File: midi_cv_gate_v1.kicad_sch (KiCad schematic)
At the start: 27 parts, among them J1 Conn_02x05_Odd_Even, J34 Conn_01x10, J35 Conn_01x10, J36 Conn_01x20, J37 Conn_01x20, J42 Conn_01x20, J43 Conn_01x20, U1 LM7805_TO220

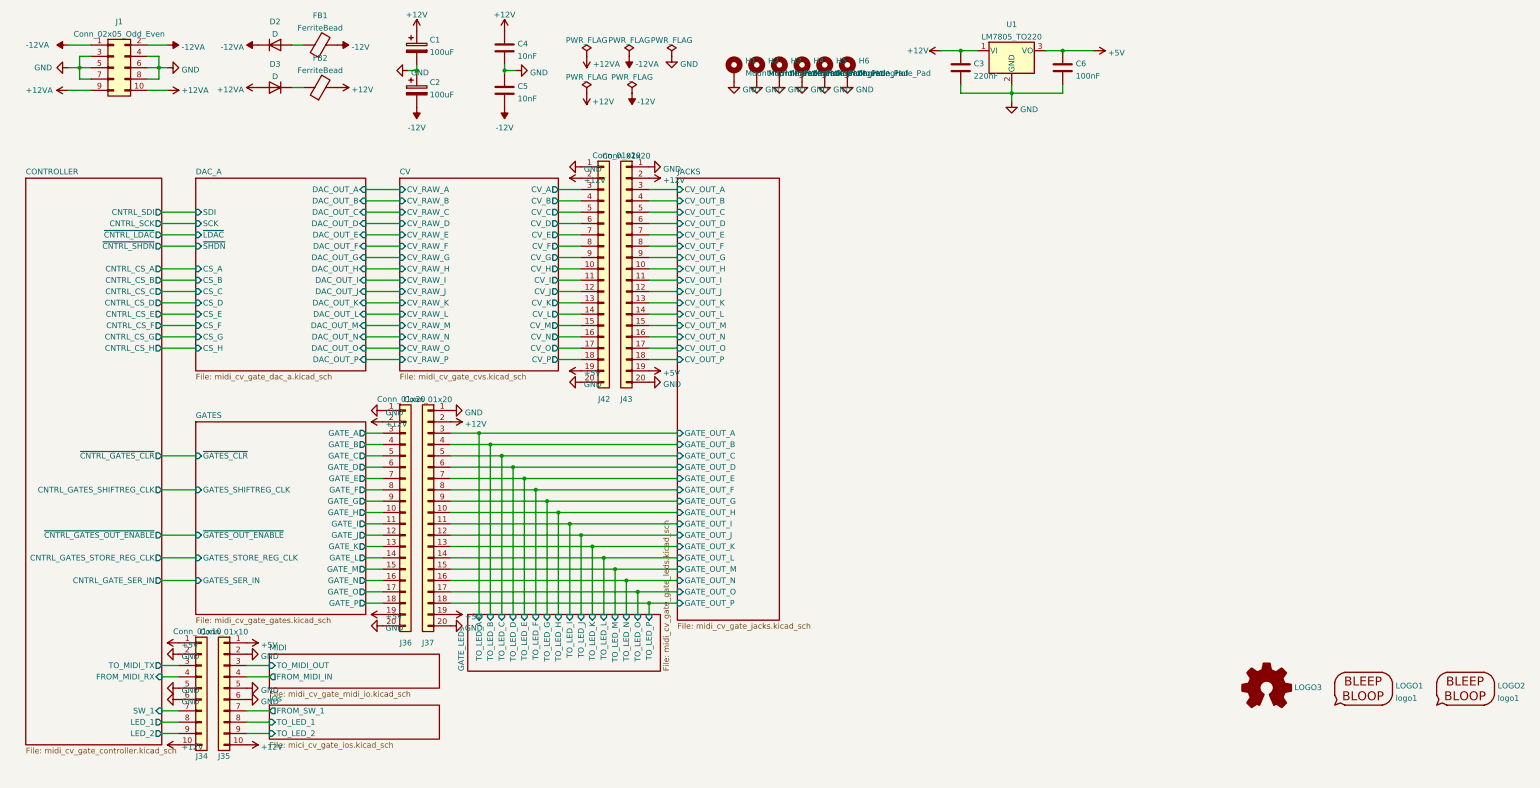
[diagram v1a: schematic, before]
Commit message: Replace soic-14 with dip 14 for DACs, add pulldowns on opamp inputs
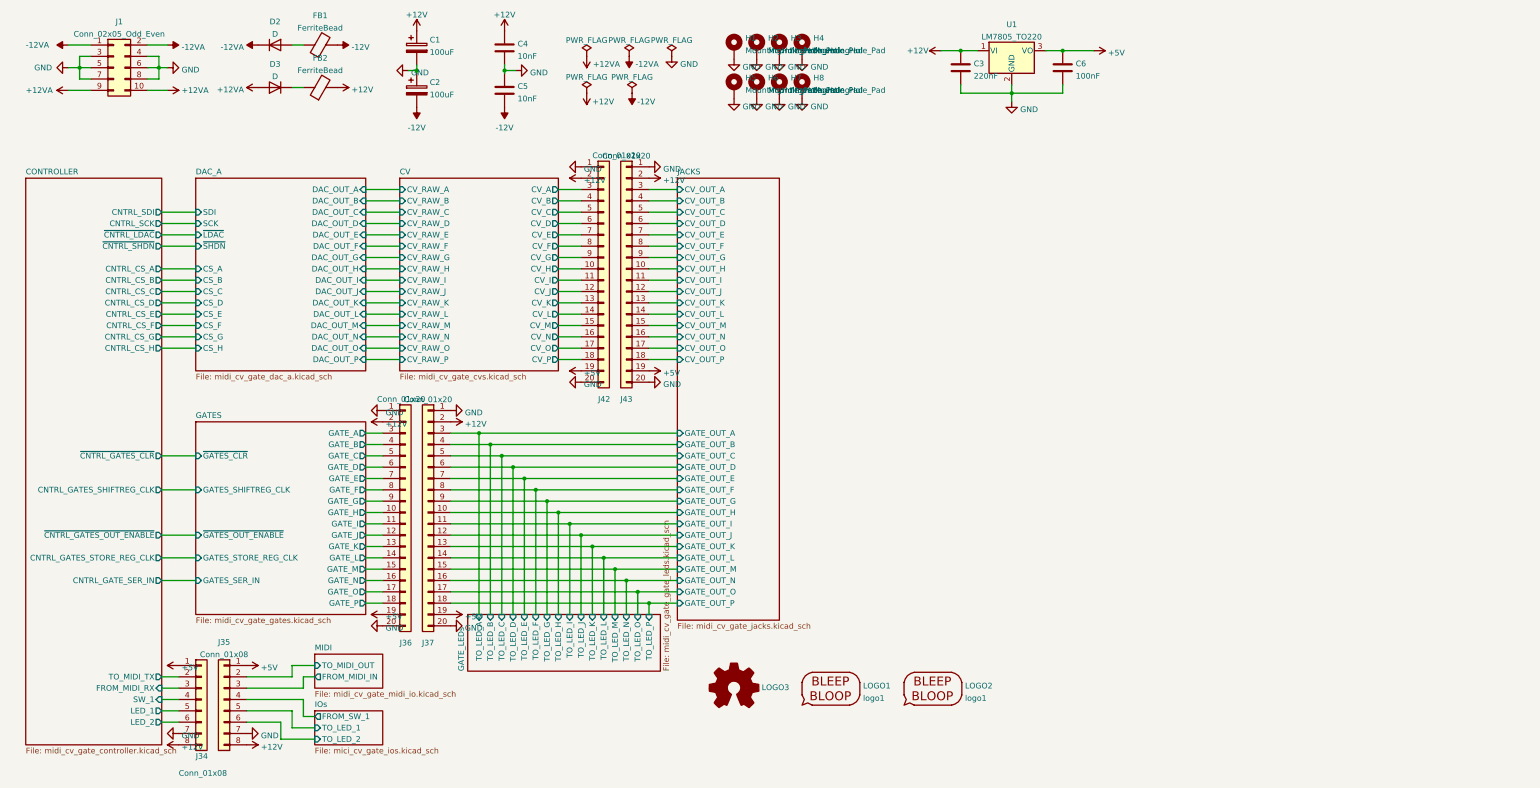
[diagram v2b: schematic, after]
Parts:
- removed J34: Conn_01x10, Connector_PinHeader_2.54mm:PinHeader_1x10_P2.54mm_Vertical, symbol Connector_Generic:Conn_01x10
- removed J35: Conn_01x10, Connector_PinSocket_2.54mm:PinSocket_1x10_P2.54mm_Vertical, symbol Connector_Generic:Conn_01x10
- added H7, H8: MountingHole_Pad, MountingHole:MountingHole_3.2mm_M3_ISO7380_Pad_TopBottom, symbol Mechanical:MountingHole_Pad
- added J34: Conn_01x08, Connector_PinHeader_2.54mm:PinHeader_1x09_P2.54mm_Vertical, symbol Connector_Generic:Conn_01x08
- added J35: Conn_01x08, Connector_PinSocket_2.54mm:PinSocket_1x08_P2.54mm_Vertical, symbol Connector_Generic:Conn_01x08
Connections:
- net +12V: now also J34.8 (Pin_8), J35.8 (Pin_8)
- net +5V: now also J34.1 (Pin_1), J35.1 (Pin_1)
- net CONTROLLER/FROM_MIDI_RX: now also J34.3 (Pin_3)
- net CONTROLLER/LED_1: now also J34.5 (Pin_5)
- net CONTROLLER/LED_2: now also J34.6 (Pin_6)
- net CONTROLLER/SW_1: now also J34.4 (Pin_4)
- net CONTROLLER/TO_MIDI_TX: now also J34.2 (Pin_2)
- net GND: now also H7.1, H8.1, J34.7 (Pin_7), J35.7 (Pin_7)
- net IOs/FROM_SW_1: now also J35.4 (Pin_4)
- net IOs/TO_LED_1: now also J35.5 (Pin_5)
- net IOs/TO_LED_2: now also J35.6 (Pin_6)
- net MIDI/FROM_MIDI_IN: now also J35.3 (Pin_3)
- net MIDI/TO_MIDI_OUT: now also J35.2 (Pin_2)
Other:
- moved on the sheet: H1, H2, H3, H4, H5, H6, LOGO1, LOGO2, LOGO3

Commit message: Partially routed
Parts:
- D2, D3: footprint Diode_THT:D_DO-35_SOD27_P7.62mm_Horizontal -> Diode_THT:D_DO-35_SOD27_P2.54mm_Vertical_KathodeUp
- FB1, FB2: footprint Inductor_THT:L_Axial_L5.3mm_D2.2mm_P7.62mm_Horizontal_Vishay_IM-1 -> Inductor_THT:L_Axial_L5.3mm_D2.2mm_P2.54mm_Vertical_Vishay_IM-1
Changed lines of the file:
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@@
     (stroke (width 0) (type default) (color 0 0 0 0))
   )
-  (wire (pts (xy 168.91 154.94) (xy 168.91 157.48))
+  (wire (pts (xy 168.91 154.94) (xy 168.91 162.56))
     (stroke (width 0) (type default) (color 0 0 0 0))
   )
@@
     (stroke (width 0) (type default) (color 0 0 0 0))
   )
-  (wire (pts (xy 163.83 149.86) (xy 163.83 157.48))
+  (wire (pts (xy 163.83 149.86) (xy 163.83 162.56))
     (stroke (width 0) (type default) (color 0 0 0 0))
   )
@@
     (stroke (width 0) (type default) (color 0 0 0 0))
   )
-  (wire (pts (xy 148.59 134.62) (xy 148.59 157.48))
+  (wire (pts (xy 148.59 134.62) (xy 148.59 162.56))
     (stroke (width 0) (type default) (color 0 0 0 0))
   )
@@
     (stroke (width 0) (type default) (color 0 0 0 0))
   )
-  (wire (pts (xy 153.67 139.7) (xy 153.67 157.48))
+  (wire (pts (xy 153.67 139.7) (xy 153.67 162.56))
     (stroke (width 0) (type default) (color 0 0 0 0))
   )
@@
     (stroke (width 0) (type default) (color 0 0 0 0))
   )
-  (wire (pts (xy 158.75 144.78) (xy 158.75 157.48))
+  (wire (pts (xy 158.75 144.78) (xy 158.75 162.56))
     (stroke (width 0) (type default) (color 0 0 0 0))
   )
@@
     (stroke (width 0) (type default) (color 0 0 0 0))
   )
-  (wire (pts (xy 161.29 147.32) (xy 161.29 157.48))
+  (wire (pts (xy 161.29 147.32) (xy 161.29 162.56))
     (stroke (width 0) (type default) (color 0 0 0 0))
   )
@@
     (stroke (width 0) (type default) (color 0 0 0 0))
   )
-  (wire (pts (xy 146.05 132.08) (xy 146.05 157.48))
+  (wire (pts (xy 146.05 132.08) (xy 146.05 162.56))
     (stroke (width 0) (type default) (color 0 0 0 0))
   )
@@
     (stroke (width 0) (type default) (color 0 0 0 0))
   )
-  (wire (pts (xy 138.43 124.46) (xy 138.43 157.48))
+  (wire (pts (xy 138.43 124.46) (xy 138.43 162.56))
     (stroke (width 0) (type default) (color 0 0 0 0))
   )
@@
     (stroke (width 0) (type default) (color 0 0 0 0))
   )
-  (wire (pts (xy 133.35 119.38) (xy 133.35 157.48))
+  (wire (pts (xy 133.35 119.38) (xy 133.35 162.56))
     (stroke (width 0) (type default) (color 0 0 0 0))
   )
@@
     (stroke (width 0) (type default) (color 0 0 0 0))
   )
-  (wire (pts (xy 151.13 137.16) (xy 151.13 157.48))
+  (wire (pts (xy 151.13 137.16) (xy 151.13 162.56))
     (stroke (width 0) (type default) (color 0 0 0 0))
   )
@@
     (stroke (width 0) (type default) (color 0 0 0 0))
   )
-  (wire (pts (xy 143.51 129.54) (xy 143.51 157.48))
+  (wire (pts (xy 143.51 129.54) (xy 143.51 162.56))
     (stroke (width 0) (type default) (color 0 0 0 0))
   )
@@
     (stroke (width 0) (type default) (color 0 0 0 0))
   )
-  (wire (pts (xy 130.81 116.84) (xy 130.81 157.48))
+  (wire (pts (xy 130.81 116.84) (xy 130.81 162.56))
     (stroke (width 0) (type default) (color 0 0 0 0))
   )
@@
     (stroke (width 0) (type default) (color 0 0 0 0))
   )
-  (wire (pts (xy 156.21 142.24) (xy 156.21 157.48))
+  (wire (pts (xy 156.21 142.24) (xy 156.21 162.56))
     (stroke (width 0) (type default) (color 0 0 0 0))
   )
@@
     (stroke (width 0) (type default) (color 0 0 0 0))
   )
-  (wire (pts (xy 140.97 127) (xy 140.97 157.48))
+  (wire (pts (xy 140.97 127) (xy 140.97 162.56))
     (stroke (width 0) (type default) (color 0 0 0 0))
   )
@@
     (stroke (width 0) (type default) (color 0 0 0 0))
   )
-  (wire (pts (xy 135.89 121.92) (xy 135.89 157.48))
+  (wire (pts (xy 135.89 121.92) (xy 135.89 162.56))
     (stroke (width 0) (type default) (color 0 0 0 0))
   )
@@
     (stroke (width 0) (type default) (color 0 0 0 0))
   )
-  (wire (pts (xy 166.37 152.4) (xy 166.37 157.48))
+  (wire (pts (xy 166.37 152.4) (xy 166.37 162.56))
     (stroke (width 0) (type default) (color 0 0 0 0))
   )
@@
     (property "Reference" "D2" (id 0) (at 85.09 24.6085 0))
     (property "Value" "D" (id 1) (at 85.09 27.3836 0))
-    (property "Footprint" "Diode_THT:D_DO-35_SOD27_P7.62mm_Horizontal" (id 2) (at 85.09 29.845 0)
+    (property "Footprint" "Diode_THT:D_DO-35_SOD27_P2.54mm_Vertical_KathodeUp" (id 2) (at 85.09 29.845 0)
       (effects (font (size 1.27 1.27)) hide)
     )
@@
     (property "Reference" "FB1" (id 0) (at 95.1992 23.2369 90))
     (property "Value" "FerriteBead" (id 1) (at 95.1992 26.012 90))
-    (property "Footprint" "Inductor_THT:L_Axial_L5.3mm_D2.2mm_P7.62mm_Horizontal_Vishay_IM-1" (id 2) (at 95.25 31.623 90)
+    (property "Footprint" "Inductor_THT:L_Axial_L5.3mm_D2.2mm_P2.54mm_Vertical_Vishay_IM-1" (id 2) (at 95.25 31.623 90)
       (effects (font (size 1.27 1.27)) hide)
     )
@@
     (property "Reference" "FB2" (id 0) (at 95.1992 32.7619 90))
     (property "Value" "FerriteBead" (id 1) (at 95.1992 35.537 90))
-    (property "Footprint" "Inductor_THT:L_Axial_L5.3mm_D2.2mm_P7.62mm_Horizontal_Vishay_IM-1" (id 2) (at 95.25 41.148 90)
+    (property "Footprint" "Inductor_THT:L_Axial_L5.3mm_D2.2mm_P2.54mm_Vertical_Vishay_IM-1" (id 2) (at 95.25 41.148 90)
       (effects (font (size 1.27 1.27)) hide)
     )
@@
     (property "Reference" "D3" (id 0) (at 85.09 34.1335 0))
     (property "Value" "D" (id 1) (at 85.09 36.9086 0))
-    (property "Footprint" "Diode_THT:D_DO-35_SOD27_P7.62mm_Horizontal" (id 2) (at 85.09 39.37 0)
+    (property "Footprint" "Diode_THT:D_DO-35_SOD27_P2.54mm_Vertical_KathodeUp" (id 2) (at 85.09 39.37 0)
       (effects (font (size 1.27 1.27)) hide)
     )
@@
     )
   )
-  (sheet (at 128.27 157.48) (size 43.18 12.7) (fields_autoplaced)
+  (sheet (at 128.27 162.56) (size 43.18 12.7)
     (stroke (width 0.1524) (type solid) (color 0 0 0 0))
     (fill (color 0 0 0 0.0000))
-    (property "Sheet name" "GATE_LEDs" (id 0) (at 127.5584 170.18 90)
+    (property "Sheet name" "GATE_LEDs" (id 0) (at 127.5584 175.26 90)
       (effects (font (size 1.27 1.27)) (justify left bottom))
     )
-    (property "Sheet file" "midi_cv_gate_gate_leds.kicad_sch" (id 1) (at 172.0346 170.18 90)
+    (property "Sheet file" "midi_cv_gate_gate_leds.kicad_sch" (id 1) (at 132.08 175.26 0)
       (effects (font (size 1.27 1.27)) (justify left top))
     )
-    (pin "TO_LED_L" input (at 158.75 157.48 90)
+    (pin "TO_LED_L" input (at 158.75 162.56 90)
       (effects (font (size 1.27 1.27)) (justify right))
     )
-    (pin "TO_LED_D" input (at 138.43 157.48 90)
+    (pin "TO_LED_D" input (at 138.43 162.56 90)
       (effects (font (size 1.27 1.27)) (justify right))
     )
-    (pin "TO_LED_H" input (at 148.59 157.48 90)
+    (pin "TO_LED_H" input (at 148.59 162.56 90)
       (effects (font (size 1.27 1.27)) (justify right))
     )
-    (pin "TO_LED_P" input (at 168.91 157.48 90)
+    (pin "TO_LED_P" input (at 168.91 162.56 90)
       (effects (font (size 1.27 1.27)) (justify right))
     )
-    (pin "TO_LED_C" input (at 135.89 157.48 90)
+    (pin "TO_LED_C" input (at 135.89 162.56 90)
       (effects (font (size 1.27 1.27)) (justify right))
     )
-    (pin "TO_LED_E" input (at 140.97 157.48 90)
+    (pin "TO_LED_E" input (at 140.97 162.56 90)
       (effects (font (size 1.27 1.27)) (justify right))
     )
-    (pin "TO_LED_I" input (at 151.13 157.48 90)
+    (pin "TO_LED_I" input (at 151.13 162.56 90)
       (effects (font (size 1.27 1.27)) (justify right))
     )
-    (pin "TO_LED_F" input (at 143.51 157.48 90)
+    (pin "TO_LED_F" input (at 143.51 162.56 90)
       (effects (font (size 1.27 1.27)) (justify right))
     )
-    (pin "TO_LED_J" input (at 153.67 157.48 90)
+    (pin "TO_LED_J" input (at 153.67 162.56 90)
       (effects (font (size 1.27 1.27)) (justify right))
     )
-    (pin "TO_LED_A" input (at 130.81 157.48 90)
+    (pin "TO_LED_A" input (at 130.81 162.56 90)
       (effects (font (size 1.27 1.27)) (justify right))
     )
-    (pin "TO_LED_B" input (at 133.35 157.48 90)
+    (pin "TO_LED_B" input (at 133.35 162.56 90)
       (effects (font (size 1.27 1.27)) (justify right))
     )
-    (pin "TO_LED_G" input (at 146.05 157.48 90)
+    (pin "TO_LED_G" input (at 146.05 162.56 90)
       (effects (font (size 1.27 1.27)) (justify right))
     )
-    (pin "TO_LED_K" input (at 156.21 157.48 90)
+    (pin "TO_LED_K" input (at 156.21 162.56 90)
       (effects (font (size 1.27 1.27)) (justify right))
     )
-    (pin "TO_LED_O" input (at 166.37 157.48 90)
+    (pin "TO_LED_O" input (at 166.37 162.56 90)
       (effects (font (size 1.27 1.27)) (justify right))
     )
-    (pin "TO_LED_N" input (at 163.83 157.48 90)
+    (pin "TO_LED_N" input (at 163.83 162.56 90)
       (effects (font (size 1.27 1.27)) (justify right))
     )
-    (pin "TO_LED_M" input (at 161.29 157.48 90)
+    (pin "TO_LED_M" input (at 161.29 162.56 90)
       (effects (font (size 1.27 1.27)) (justify right))
     )
@@
     )
     (path "/06f573de-ffb2-4af5-8c31-cc321694122a"
-      (reference "D2") (unit 1) (value "D") (footprint "Diode_THT:D_DO-35_SOD27_P7.62mm_Horizontal")
+      (reference "D2") (unit 1) (value "D") (footprint "Diode_THT:D_DO-35_SOD27_P2.54mm_Vertical_KathodeUp")
     )
     (path "/f2e5238c-7c0a-43f2-8586-2556d40d458e"
-      (reference "D3") (unit 1) (value "D") (footprint "Diode_THT:D_DO-35_SOD27_P7.62mm_Horizontal")
+      (reference "D3") (unit 1) (value "D") (footprint "Diode_THT:D_DO-35_SOD27_P2.54mm_Vertical_KathodeUp")
     )
     (path "/e0c84674-31e6-4d06-a99e-e9f0c7d90780/91050ba3-e03c-46c0-bc91-93c9d8a04d56"
@@
     )
     (path "/3c5c2fda-68a3-437c-bc2c-ea7802ac1a5e"
-      (reference "FB1") (unit 1) (value "FerriteBead") (footprint "Inductor_THT:L_Axial_L5.3mm_D2.2mm_P7.62mm_Horizontal_Vishay_IM-1")
+      (reference "FB1") (unit 1) (value "FerriteBead") (footprint "Inductor_THT:L_Axial_L5.3mm_D2.2mm_P2.54mm_Vertical_Vishay_IM-1")
     )
     (path "/b476715f-cc57-4130-a5cd-755f3641ef0b"
-      (reference "FB2") (unit 1) (value "FerriteBead") (footprint "Inductor_THT:L_Axial_L5.3mm_D2.2mm_P7.62mm_Horizontal_Vishay_IM-1")
+      (reference "FB2") (unit 1) (value "FerriteBead") (footprint "Inductor_THT:L_Axial_L5.3mm_D2.2mm_P2.54mm_Vertical_Vishay_IM-1")
     )
     (path "/fc885f62-14ee-403a-8f02-c04ec13415e6"

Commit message: Routing of main board done
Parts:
- J34: footprint Connector_PinHeader_2.54mm:PinHeader_1x09_P2.54mm_Vertical -> Connector_PinHeader_2.54mm:PinHeader_1x08_P2.54mm_Vertical
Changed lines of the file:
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@@
       (effects (font (size 1.27 1.27)) (justify left))
     )
-    (property "Footprint" "Connector_PinHeader_2.54mm:PinHeader_1x09_P2.54mm_Vertical" (id 2) (at 68.58 176.53 0)
+    (property "Footprint" "Connector_PinHeader_2.54mm:PinHeader_1x08_P2.54mm_Vertical" (id 2) (at 68.58 176.53 0)
       (effects (font (size 1.27 1.27)) hide)
     )
@@
     )
     (path "/990f515d-4c7b-464d-a276-c2f3ab1de114"
-      (reference "J34") (unit 1) (value "Conn_01x08") (footprint "Connector_PinHeader_2.54mm:PinHeader_1x09_P2.54mm_Vertical")
+      (reference "J34") (unit 1) (value "Conn_01x08") (footprint "Connector_PinHeader_2.54mm:PinHeader_1x08_P2.54mm_Vertical")
     )
     (path "/b11d063a-dff6-4b5a-8aba-d116b85efc6e"
@@
       (reference "SW1") (unit 1) (value "SW_SPST") (footprint "My Stuff:SW_PS1024ALRED")
     )
+    (path "/c47bc308-08b7-43ac-902b-762d7bd38681/3b1e74a1-6d79-400b-921d-bca8daacf555"
+      (reference "TP6") (unit 1) (value "QH_1") (footprint "TestPoint:TestPoint_Pad_D1.0mm")
+    )
     (path "/c47bc308-08b7-43ac-902b-762d7bd38681/a9987a6c-fb6e-4fe3-b37f-366c5d0b0a30"
-      (reference "TP1") (unit 1) (value "TestPoint") (footprint "TestPoint:TestPoint_Pad_D1.0mm")
+      (reference "TP7") (unit 1) (value "QH2") (footprint "TestPoint:TestPoint_Pad_D1.0mm")
     )
     (path "/95d1bf8a-86c3-4127-b39f-a83020e3ac99"
